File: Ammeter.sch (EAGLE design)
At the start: 83 parts, among them IC1 TL081P, IC2 TL081P, IC3 ICL7107, IC4 TL081P, IC5 TL081P, IC6 TL081P, IC7 TL081P, IC8 TL081P, IC9 TL081P, T1 BD139

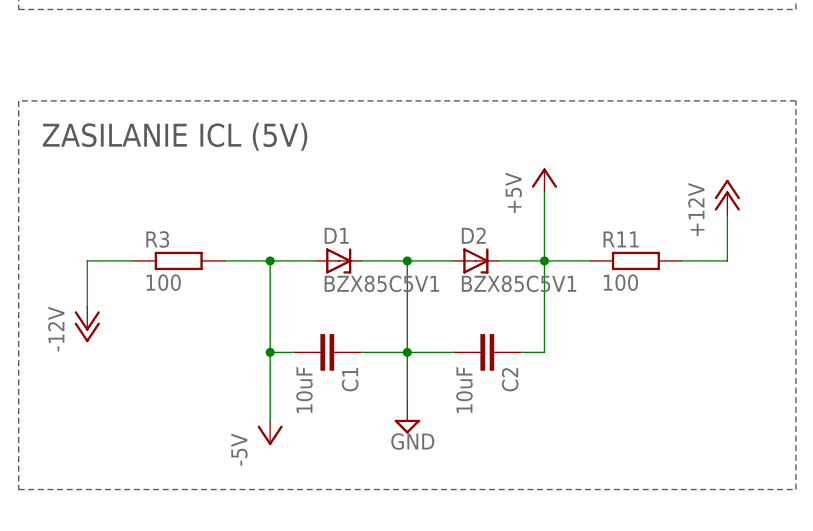
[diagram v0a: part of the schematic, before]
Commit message: hotfix: updated R3 an R11 values
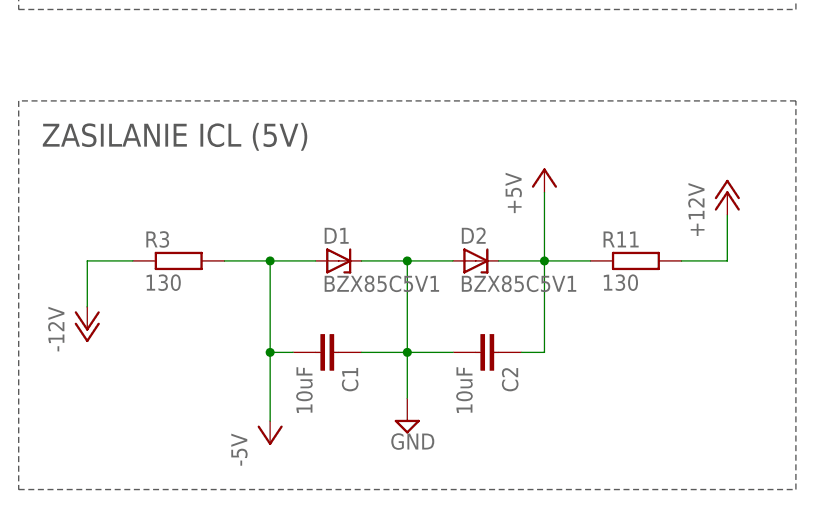
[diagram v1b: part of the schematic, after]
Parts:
- R11, R3: value 100 -> 130
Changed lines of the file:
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@@
 <part name="G2" library="battery" library_urn="urn:adsk.eagle:library:109" deviceset="CH291-1220LF" device="" package3d_urn="urn:adsk.eagle:package:4617/1" value="12V"/>
 <part name="G1" library="battery" library_urn="urn:adsk.eagle:library:109" deviceset="CH291-1220LF" device="" package3d_urn="urn:adsk.eagle:package:4617/1" value="12V"/>
-<part name="R3" library="resistor" library_urn="urn:adsk.eagle:library:348" deviceset="R-EU_" device="0204/7" package3d_urn="urn:adsk.eagle:package:25945/1" value="100"/>
+<part name="R3" library="resistor" library_urn="urn:adsk.eagle:library:348" deviceset="R-EU_" device="0204/7" package3d_urn="urn:adsk.eagle:package:25945/1" value="130"/>
 <part name="SUPPLY4" library="supply2" library_urn="urn:adsk.eagle:library:372" deviceset="GND" device=""/>
 <part name="C1" library="resistor" library_urn="urn:adsk.eagle:library:348" deviceset="C-EU" device="025-024X044" package3d_urn="urn:adsk.eagle:package:26149/1" value="10uF"/>
 <part name="C2" library="resistor" library_urn="urn:adsk.eagle:library:348" deviceset="C-EU" device="025-024X044" package3d_urn="urn:adsk.eagle:package:26149/1" value="10uF"/>
-<part name="R11" library="resistor" library_urn="urn:adsk.eagle:library:348" deviceset="R-EU_" device="0204/7" package3d_urn="urn:adsk.eagle:package:25945/1" value="100"/>
+<part name="R11" library="resistor" library_urn="urn:adsk.eagle:library:348" deviceset="R-EU_" device="0204/7" package3d_urn="urn:adsk.eagle:package:25945/1" value="130"/>
 <part name="P+4" library="supply1" library_urn="urn:adsk.eagle:library:371" deviceset="+5V" device=""/>
 <part name="P-3" library="supply1" library_urn="urn:adsk.eagle:library:371" deviceset="-5V" device=""/>
